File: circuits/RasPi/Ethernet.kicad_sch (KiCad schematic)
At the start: 4 parts, among them J7 RJ45_Hanrun_HR911105A_Horizon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

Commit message: panelフットプリント配置
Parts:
- J7: footprint (none) -> MyLibrary:Connector_RJ45_LPJK7001AGNL
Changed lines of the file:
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@@
       (effects (font (size 1.27 1.27)))
     )
-    (property "Footprint" "" (at 149.86 53.34 0)
+    (property "Footprint" "MyLibrary:Connector_RJ45_LPJK7001AGNL" (at 149.86 53.34 0)
       (effects (font (size 1.27 1.27)) hide)
     )

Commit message: シンボル・フットプリントMyLib->TomoshibiLib置き換え
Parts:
- J7: footprint MyLibrary:Connector_RJ45_LPJK7001AGNL -> TomoshibiLibrary:Connector_RJ45_LPJK7001AGNL
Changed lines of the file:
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@@
       (effects (font (size 1.27 1.27)))
     )
-    (property "Footprint" "MyLibrary:Connector_RJ45_LPJK7001AGNL" (at 149.86 53.34 0)
+    (property "Footprint" "TomoshibiLibrary:Connector_RJ45_LPJK7001AGNL" (at 149.86 53.34 0)
       (effects (font (size 1.27 1.27)) hide)
     )

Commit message: 更新
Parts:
- J7: value RJ45_Hanrun_HR911105A_Horizontal -> RJ45_LPJK7001AGNL
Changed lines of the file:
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@@
       (effects (font (size 1.27 1.27)))
     )
-    (property "Value" "RJ45_Hanrun_HR911105A_Horizontal" (at 151.13 54.61 0)
+    (property "Value" "RJ45_LPJK7001AGNL" (at 151.13 54.61 0)
       (effects (font (size 1.27 1.27)))
     )
@@
     (pin "13")
     (pin "12")
+    (pin "16")
     (pin "14")
     (pin "15")
-    (pin "16")
     (instances
       (project "RasPi"

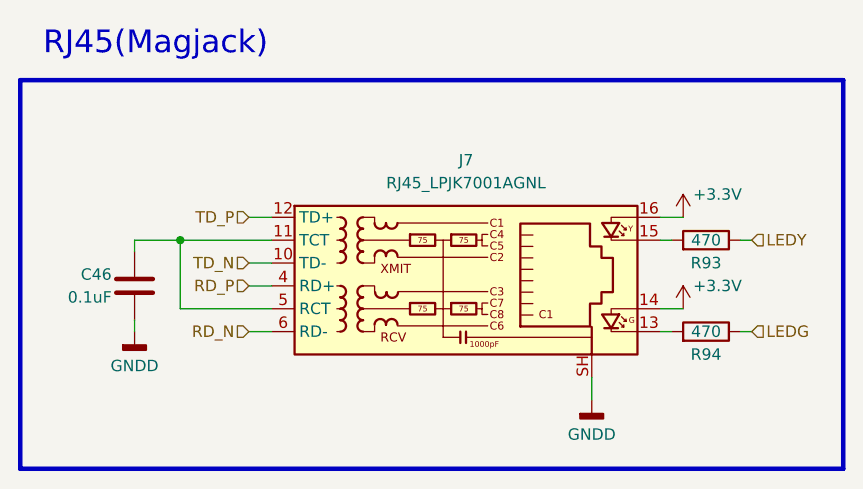
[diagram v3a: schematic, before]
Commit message: 発注第2弾
RasPi発注
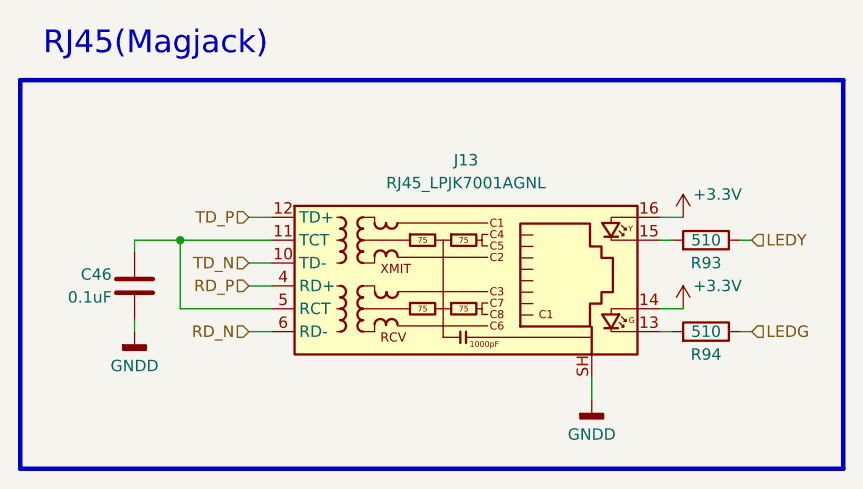
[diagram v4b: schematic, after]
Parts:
- R93, R94: value 470 -> 510
- renumbered J7 to J13
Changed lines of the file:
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@@
       (effects (font (size 1.27 1.27)))
     )
-    (property "Value" "470" (at 177.8 71.12 90)
+    (property "Value" "510" (at 177.8 71.12 90)
       (effects (font (size 1.27 1.27)))
     )
@@
   (symbol (lib_id "Connector:RJ45_Hanrun_HR911105A_Horizontal") (at 149.86 66.04 0) (unit 1)
     (in_bom yes) (on_board yes) (dnp no) (fields_autoplaced)
-    (property "Reference" "J7" (at 151.13 52.07 0)
+    (property "Reference" "J13" (at 151.13 52.07 0)
       (effects (font (size 1.27 1.27)))
     )
@@
       (project "RasPi"
         (path "/689a9e74-f202-4ea4-bfbb-4341f2549250/fddad0c3-2af8-46e3-8794-fa1122d24d51/2743e81b-c35a-4f5b-a403-d8487e16cd8c"
-          (reference "J7") (unit 1)
+          (reference "J13") (unit 1)
         )
       )
@@
       (effects (font (size 1.27 1.27)))
     )
-    (property "Value" "470" (at 177.8 60.96 90)
+    (property "Value" "510" (at 177.8 60.96 90)
       (effects (font (size 1.27 1.27)))
     )
